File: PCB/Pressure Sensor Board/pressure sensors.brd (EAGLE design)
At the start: 34.9 x 34.9 mm, 4 parts

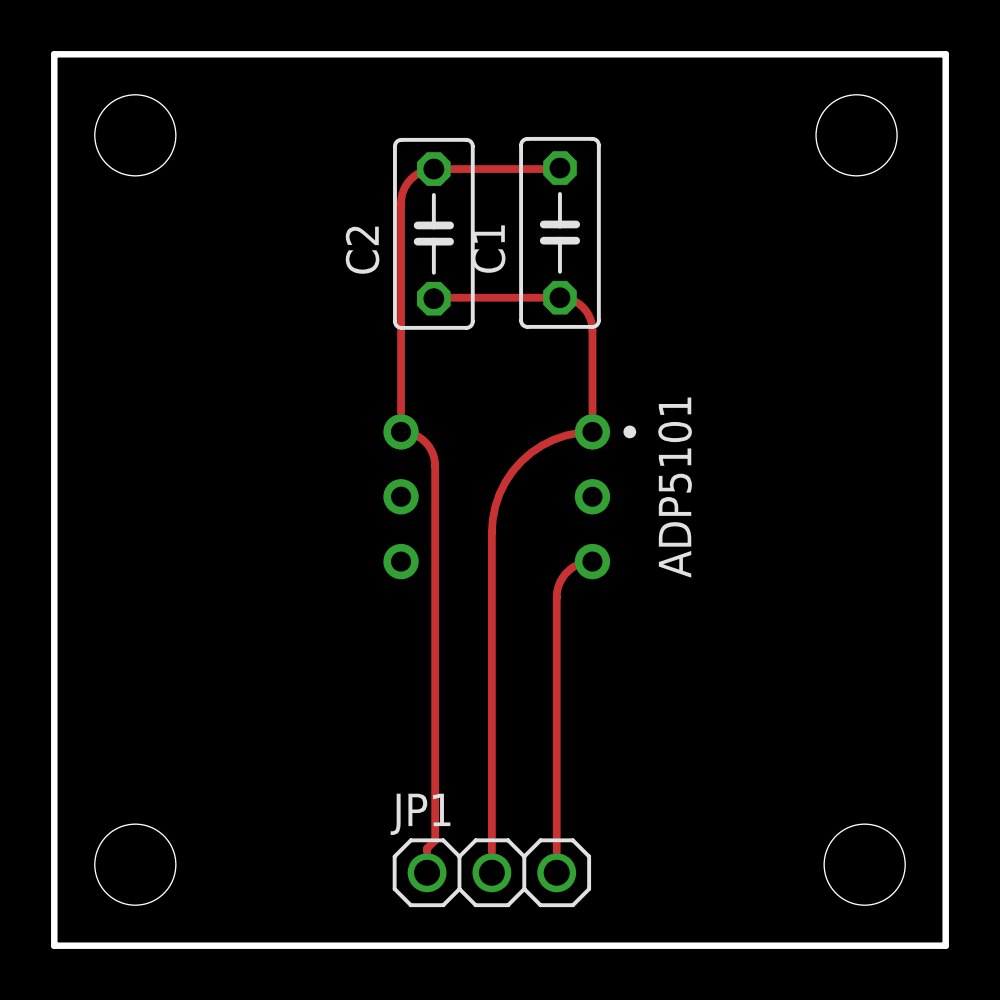
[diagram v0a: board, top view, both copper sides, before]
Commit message: Added Images of PCBs and sorted
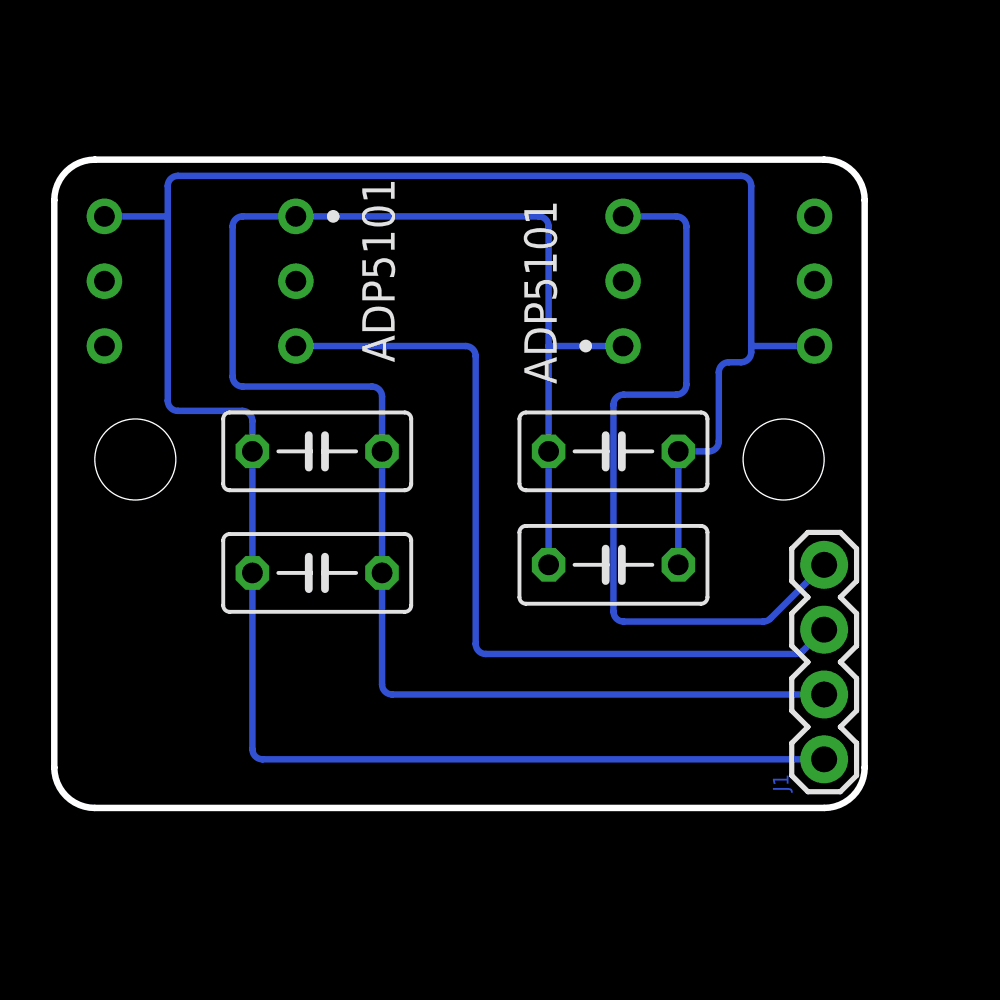
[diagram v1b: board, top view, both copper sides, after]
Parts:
- removed JP1: (no value), adafruit:1X03
- added C3: 1µF, rcl:C050-030X075
- added C4: 1nF, rcl:C050-030X075
- added J1: (no value), SparkFun-Connectors:1X04
- added U$2: ADP5101, local eagle library:DIP750W53P254L720H850Q6B
- U$1: value ADP5101 -> 1
- moved U$1 14.4 mm to (5.71, -8.89)
- moved C1 13.2 mm to (21.9, -20.0), turned to 0 degrees
- moved C2 11.1 mm to (21.9, -15.6), turned to 0 degrees
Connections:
- removed net N$1: C1.1, C2.1, JP1.2, U$1.1
- removed net N$2: C1.2, C2.2, JP1.1, U$1.6
- new net 5V: C1.1, C2.1, C3.1, C4.1, J1.2, U$1.1, U$2.1
- new net GND: C1.2, C2.2, C3.2, C4.2, J1.1, U$1.6, U$2.6
- new net N$6: J1.4, U$2.3
- net N$3: now also J1.3; no longer JP1.3
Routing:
- net GND: track 0.00 -> 92.6 mm
- net 5V: track 0.00 -> 69.7 mm
- net N$2: track 33.8 -> 0.00 mm
- net N$1: track 29.9 -> 0.00 mm
- net N$6: track 0.00 -> 29.4 mm
- net N$3: track 12.8 -> 32.7 mm
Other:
- board size 34.9 x 34.9 mm -> 31.8 x 25.4 mm
